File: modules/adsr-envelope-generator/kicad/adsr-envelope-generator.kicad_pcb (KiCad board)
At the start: 2 copper layers, 78 parts, among them P1 CONN_01X03, P2 CONN_01X02, P3 CONN_01X02, P4 CONN_01X03, Q1 Q_NPN_EBC, Q2 Q_NPN_EBC, Q3 Q_NPN_EBC, U1 TL074, U2 4066, U3 40106, U4 TL074, U5 4001

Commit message: ADSR PCB by freerouter
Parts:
- C1, C10, C11, C12, C13, C14, C15, C16, C17, C18, C19, C2, C20, C3, C4, C5, C6, C7, C8, C9, D1, D2, D3, D4, D5, D6, D7, D8, D9, P1, P2, P3, P4, Q1, Q2, Q3, R1, R10, R11, R12, R13, R14, R15, R16, R17, R18, R19, R2, R20, R21, R22, R23, R24, R25, R26, R27, R28, R29, R3, R30, R31, R32, R33, R4, R5, R6, R7, R8, R9, U1, U2, U3, U4, U5: moved to B.Cu
- moved R1 105.6 mm to (80.5, 98.8), turned to 270 degrees
- moved R2 99.5 mm to (82.5, 84.3), turned to 180 degrees
- moved R3 90.4 mm to (80.5, 90.4), turned to 270 degrees
- moved C15 88.3 mm to (83.3, 80.5)
- moved R4 84.2 mm to (80.5, 114.6), turned to 270 degrees
- moved R11 79.0 mm to (84.6, 90.7), turned to 270 degrees
- moved Q2 76.0 mm to (110.7, 84.3)
- moved U1 73.5 mm to (117.3, 100.1), turned to 270 degrees
- moved R12 72.8 mm to (84.6, 98.8), turned to 270 degrees
- moved R13 72.0 mm to (80.5, 106.7), turned to 270 degrees
- moved R8 71.2 mm to (84.3, 106.9), turned to 270 degrees
- moved R5 70.7 mm to (84.6, 114.6), turned to 270 degrees
- moved R28 64.7 mm to (115.6, 90.4), turned to 270 degrees
- moved R29 64.6 mm to (111.0, 100.1), turned to 270 degrees
- moved C13 64.5 mm to (127.3, 103.9)
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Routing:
- net GND: track 0.00 -> 328.3 mm, vias 0 -> 2
- net VCC: track 0.00 -> 225.0 mm, vias 0 -> 5
- net Net-(C3-Pad1): track 0.00 -> 139.8 mm, vias 0 -> 3
- net VEE: track 0.00 -> 133.0 mm, vias 0 -> 4
- net Net-(C5-Pad1): track 0.00 -> 132.2 mm, vias 0 -> 3
- net Net-(C4-Pad1): track 0.00 -> 120.9 mm, vias 0 -> 4
- net GateInput: track 0.00 -> 116.6 mm, vias 0 -> 2
- net OutputLevel: track 0.00 -> 114.3 mm, vias 0 -> 2
- net Net-(C5-Pad2): track 0.00 -> 105.8 mm, vias 0 -> 3
- net Net-(C9-Pad1): track 0.00 -> 103.1 mm, vias 0 -> 4
- net TriggerInput: track 0.00 -> 99.1 mm, vias 0 -> 1
- net ManTriggerBTN: track 0.00 -> 94.3 mm
- net Net-(Q1-Pad2): track 0.00 -> 90.8 mm, vias 0 -> 2
- net Net-(C2-Pad2): track 0.00 -> 86.4 mm, vias 0 -> 3
- net Net-(D3-Pad2): track 0.00 -> 84.4 mm, vias 0 -> 2
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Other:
- board outline added: 73.2 x 49.8 mm

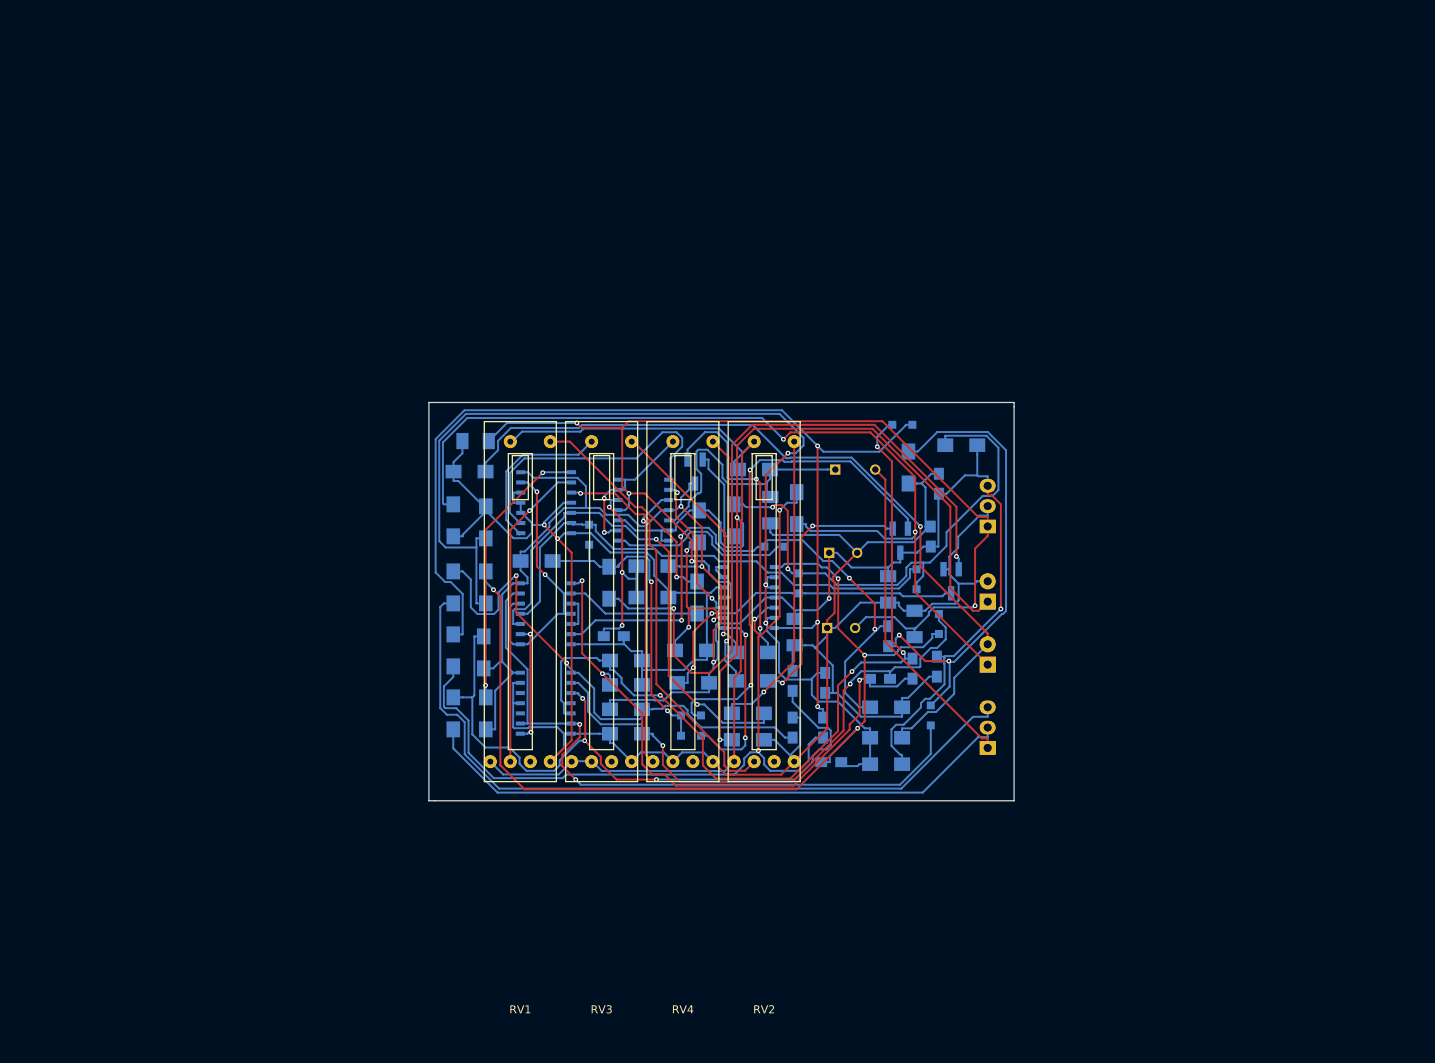
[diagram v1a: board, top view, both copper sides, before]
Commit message: Redo ADSR generator PCB layout
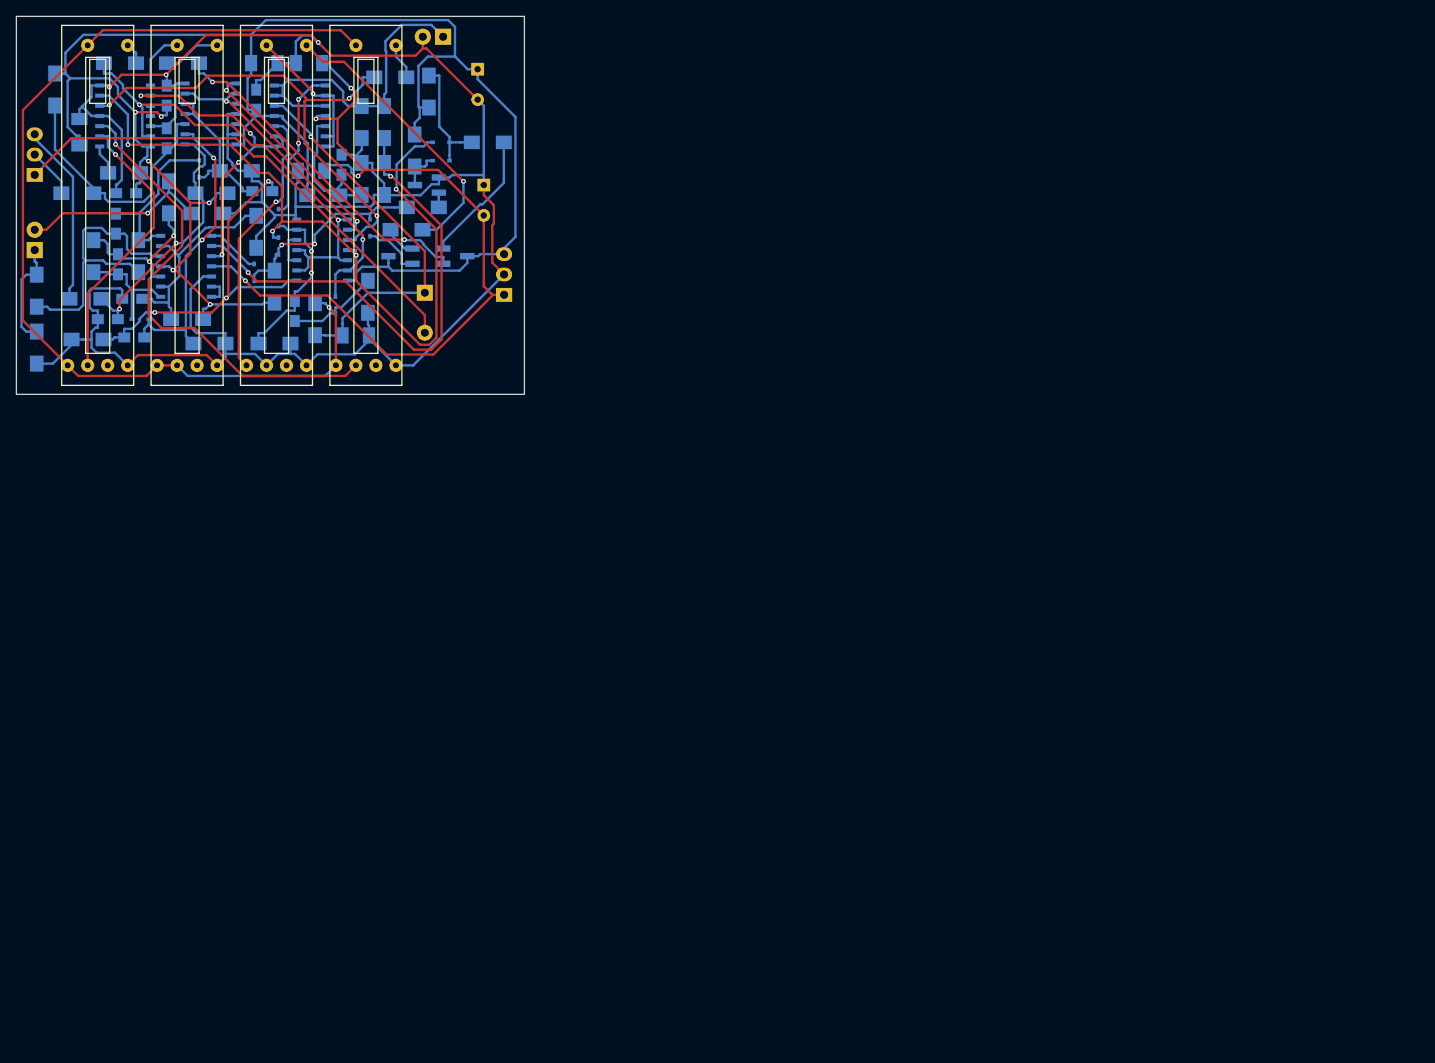
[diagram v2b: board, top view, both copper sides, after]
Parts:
- C12, C13: footprint Capacitors_ThroughHole:C_Radial_D8_L11.5_P3.5 -> Capacitors_ThroughHole:CP_Radial_D8.0mm_P3.80mm
- C8: footprint Capacitors_ThroughHole:C_Radial_D10_L13_P5 -> Capacitors_ThroughHole:CP_Radial_D10.0mm_P5.00mm
- D1, D2, D3, D4, D5, D6, D7, D8, D9: footprint Diodes_SMD:SOD-323_HandSoldering -> Diodes_SMD:SOD-323
- moved P1 139.0 mm to (28.2, 47.2)
- moved P2 129.9 mm to (28.2, 56.6)
- moved C18 119.8 mm to (44.7, 37.3), turned to 270 degrees
- moved C16 116.1 mm to (33.8, 41.9), turned to 90 degrees
- moved R9 112.3 mm to (45.0, 50.0), turned to 90 degrees
- moved C19 109.4 mm to (39.6, 49.5), turned to 0 degrees
- moved C4 108.7 mm to (38.6, 58.4), turned to 90 degrees
- moved C5 108.5 mm to (38.4, 53.3)
- moved D1 106.8 mm to (41.4, 65.3), turned to 180 degrees
- moved R6 103.6 mm to (47.2, 65.3)
- moved C2 103.5 mm to (44.7, 42.7)
- moved C7 102.5 mm to (40.6, 67.6)
- moved R30 102.4 mm to (46.7, 33.3)
- moved C9 100.8 mm to (56.6, 49.3), turned to 0 degrees
- moved C1 99.7 mm to (37.3, 65.3), turned to 0 degrees
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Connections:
- C4 pad 2: Net-(C3-Pad1) -> Net-(C4-Pad2)
- R12 pad 2: Net-(C3-Pad1) -> Net-(C4-Pad2)
- R9 pad 1: Net-(C3-Pad1) -> Net-(C4-Pad2)
- U1 pad 3: Net-(C3-Pad1) -> Net-(C4-Pad2)
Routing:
- net Net-(C3-Pad1): track 139.8 -> 27.8 mm, vias 3 -> 0
- net Net-(C5-Pad1): track 132.2 -> 21.2 mm, vias 3 -> 0
- net Net-(C4-Pad1): track 120.9 -> 14.1 mm, vias 4 -> 0
- net GateInput: track 116.6 -> 13.4 mm, vias 2 -> 0
- net Net-(Q1-Pad2): track 90.8 -> 1.85 mm, vias 2 -> 0
- net Net-(C9-Pad1): track 103.1 -> 20.2 mm, vias 4 -> 0
- net TriggerInput: track 99.1 -> 24.1 mm
- net OutputLevel: track 114.3 -> 41.1 mm, vias 2 -> 0
- net ManTriggerBTN: track 94.3 -> 22.7 mm
- net Net-(C5-Pad2): track 105.8 -> 35.2 mm, vias 3 -> 0
- net ManGateBTN: track 75.5 -> 6.21 mm
- net Net-(D9-Pad1): track 62.4 -> 7.47 mm, vias 2 -> 0
- net Net-(C2-Pad2): track 86.4 -> 33.0 mm, vias 3 -> 0
- net Net-(C10-Pad1): track 74.2 -> 22.0 mm, vias 4 -> 2
- net Net-(D5-Pad2): track 65.7 -> 15.3 mm, vias 2 -> 0
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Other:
- board size 73.2 x 49.8 mm -> 63.5 x 47.2 mm
- net class Default: clearance 0.2 -> 0.3; trace_width 0.25 -> 0.3
- rule pad_to_mask_clearance: 0.2 -> 0
- rule trace_clearance: 0.2 -> 0.3
- board text added: "+"
- board text added: "-"
- board text added: "0"
- board text added: "ADSR EG MICHD, JAN 2017"
- board text added: "ADSR OUT"
- board text added: "BASED ON RAY WILSON'S CIRCUIT DESIGN"
- board text added: "GateIn"
- board text added: "Lsw"
- board text added: "TrigIn"
- board text added: "mG"
- board text added: "mT"

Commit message: Finish up ADSR generator schematic, PCB, replace broken one
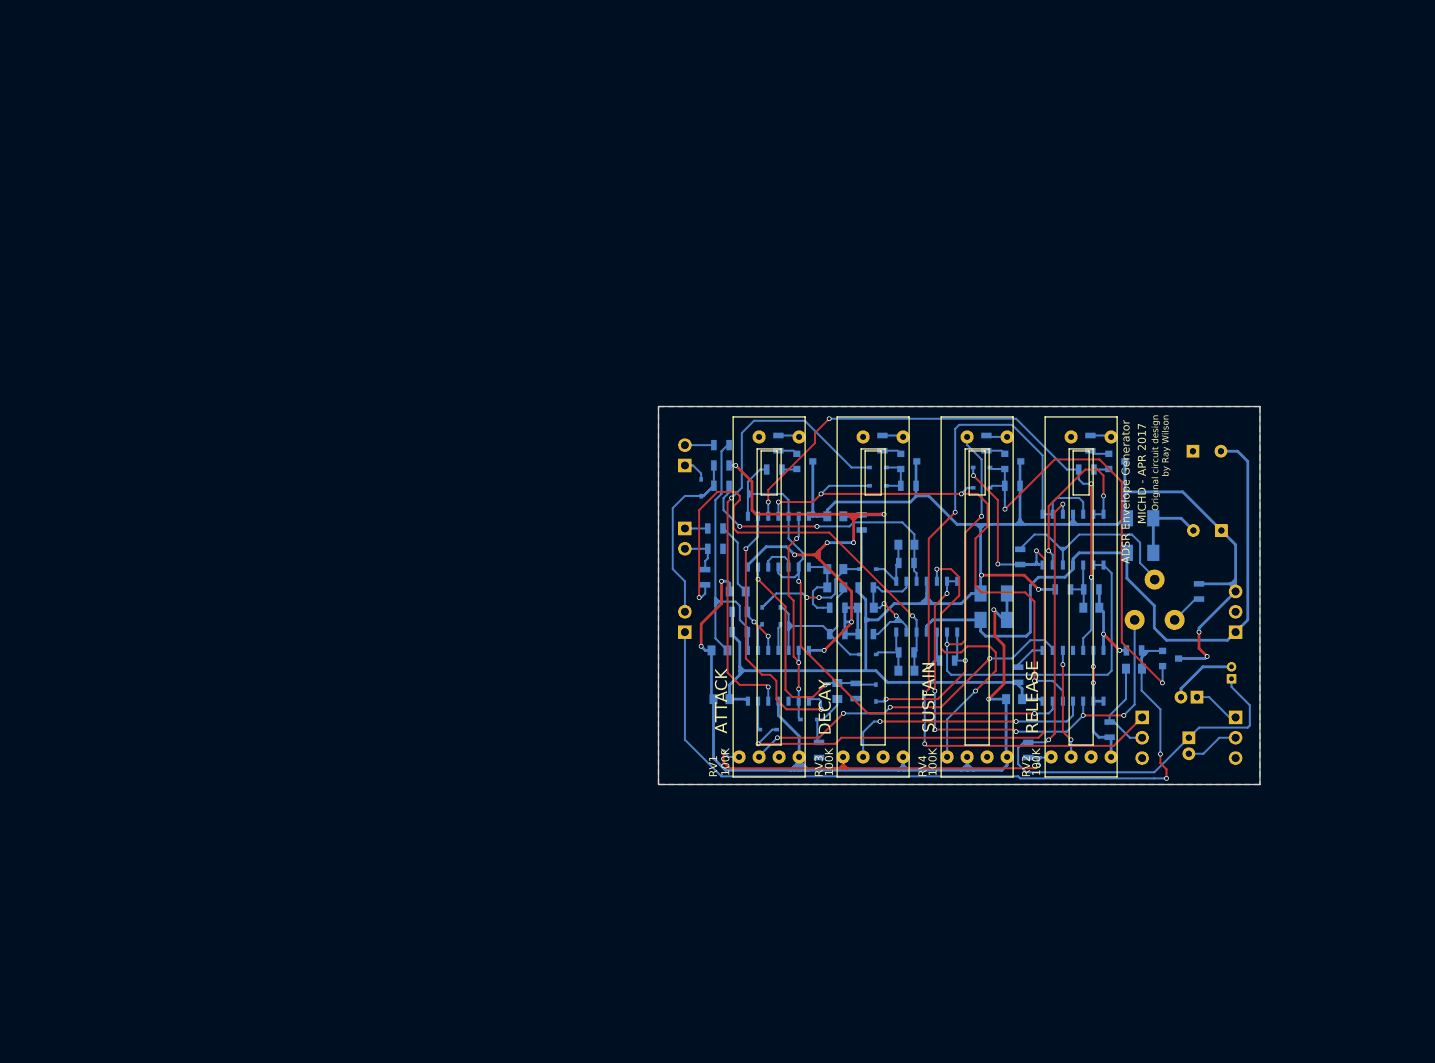
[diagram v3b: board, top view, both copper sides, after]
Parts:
- added C21: 10n, Capacitors_SMD:C_0805, B.Cu at (165.6, 109.0)
- added C22: 100n, Capacitors_SMD:C_0805, B.Cu at (114.0, 112.8)
- added D10: 1N4148, Diodes_SMD:SOD-323, B.Cu at (146.6, 83.8)
- added D11: 1N4148, Diodes_SMD:SOD-323, B.Cu at (146.6, 86.4)
- added D12: 1N4148, Diodes_SMD:SOD-323, B.Cu at (111.5, 86.4)
- added P5: CONN_01X03, Pin_Headers:Pin_Header_Straight_1x03_Pitch2.54mm, B.Cu at (166.6, 115.1)
- added P6: CONN_01X02, Pin_Headers:Pin_Header_Straight_1x02_Pitch2.54mm, B.Cu at (109.5, 104.4)
- added Q4: MMBT3904, TO_SOT_Packages_SMD:SOT-23, B.Cu at (150.5, 83.1)
- added Q5: MMBT3904, TO_SOT_Packages_SMD:SOT-23, B.Cu at (163.5, 83.1)
- added R34: 220R, Resistors_SMD:R_0805, B.Cu at (160.2, 80.8)
- added RV5: 10K, Potentiometers:Potentiometer_Triwood_RM-065, B.Cu at (170.7, 102.9)
- C1, C19, C2, C20, C3, C4, C5, C7: footprint Capacitors_SMD:C_0805_HandSoldering -> Capacitors_SMD:C_0805
- C10: value 1n -> 47u; footprint Capacitors_SMD:C_0805_HandSoldering -> Capacitors_ThroughHole:CP_Radial_D5.0mm_P2.00mm
- C11: value 100n -> 1n; footprint Capacitors_SMD:C_0805_HandSoldering -> Capacitors_SMD:C_0805
- C12, C13: footprint Capacitors_ThroughHole:CP_Radial_D8.0mm_P3.80mm -> Capacitors_ThroughHole:CP_Radial_D8.0mm_P3.50mm
- C14: value 10u -> 100n; footprint SMD_Packages:SMD-1206_Pol -> Capacitors_SMD:C_0805
- C18: value 100n -> 10u; footprint Capacitors_SMD:C_0805_HandSoldering -> SMD_Packages:SMD-1206_Pol
- C6: value 10u -> 3.3u; footprint SMD_Packages:SMD-1206_Pol -> Capacitors_ThroughHole:CP_Radial_D4.0mm_P1.50mm
- C8: value 220u -> 10n; footprint Capacitors_ThroughHole:CP_Radial_D10.0mm_P5.00mm -> Capacitors_SMD:C_0805
- C9: value 1n -> 100u; footprint Capacitors_SMD:C_0805_HandSoldering -> Capacitors_ThroughHole:CP_Radial_D5.0mm_P2.00mm
- P1: value CONN_01X03 -> CONN_01X02; footprint Pin_Headers:Pin_Header_Straight_1x03 -> Pin_Headers:Pin_Header_Straight_1x02_Pitch2.54mm
- P2: footprint Pin_Headers:Pin_Header_Straight_1x02 -> Pin_Headers:Pin_Header_Straight_1x02_Pitch2.54mm
- P3: value CONN_01X02 -> CONN_01X03; footprint Pin_Headers:Pin_Header_Straight_1x02 -> Pin_Headers:Pin_Header_Straight_1x03_Pitch2.54mm
- P4: footprint Pin_Headers:Pin_Header_Straight_1x03 -> Pin_Headers:Pin_Header_Straight_1x03_Pitch2.54mm
- Q1, Q2, Q3: value Q_NPN_EBC -> MMBT3904; footprint TO_SOT_Packages_SMD:SOT-23_Handsoldering -> TO_SOT_Packages_SMD:SOT-23
- R1: value 1K -> 100R; footprint Resistors_SMD:R_1206_HandSoldering -> Resistors_SMD:R_0805
- R10, R9: value 20K -> 10K; footprint Resistors_SMD:R_1206_HandSoldering -> Resistors_SMD:R_0805
- R11, R12, R13, R14, R15, R16, R17, R18, R19, R2, R25, R27, R28, R3, R31, R32, R8: footprint Resistors_SMD:R_1206_HandSoldering -> Resistors_SMD:R_0805
- R20: value 100K -> 1M; footprint Resistors_SMD:R_1206_HandSoldering -> Resistors_SMD:R_0805
- R21: value 100K -> 10K; footprint Resistors_SMD:R_1206_HandSoldering -> Resistors_SMD:R_0805
- R22: value 2K2 -> 33K; footprint Resistors_SMD:R_1206_HandSoldering -> Resistors_SMD:R_0805
- R23, R26: value 10K -> 100K; footprint Resistors_SMD:R_1206_HandSoldering -> Resistors_SMD:R_0805
- R24: value 82K -> 1M; footprint Resistors_SMD:R_1206_HandSoldering -> Resistors_SMD:R_0805
- R29, R30: value 220R -> 10K; footprint Resistors_SMD:R_1206_HandSoldering -> Resistors_SMD:R_0805
- R33: value 10K -> 220R; footprint Resistors_SMD:R_1206_HandSoldering -> Resistors_SMD:R_0805
- R4: value 1K -> 33K; footprint Resistors_SMD:R_1206_HandSoldering -> Resistors_SMD:R_0805
- R5: value 100R -> 1K; footprint Resistors_SMD:R_1206_HandSoldering -> Resistors_SMD:R_0805
- R6: value 33K -> 22K; footprint Resistors_SMD:R_1206_HandSoldering -> Resistors_SMD:R_0805
- R7: value 1K -> 22K; footprint Resistors_SMD:R_1206_HandSoldering -> Resistors_SMD:R_0805
- RV1, RV2, RV3, RV4: value LED-POT -> 100K; footprint Bourns PTL:Bourns PTL30-X -> Bourns PTL:Bourns-PTL30-X
- U1: value TL074 -> 4066
- U2: value 4066 -> TL974
- U4: value TL074 -> 4001
- U5: value 4001 -> TL974
- moved C9 134.5 mm to (172.5, 117.6), turned to 270 degrees
- moved C18 134.4 mm to (166.4, 94.5), turned to 180 degrees
- moved P3 130.6 mm to (178.3, 115.1), turned to 180 degrees
- moved C16 129.5 mm to (148.1, 102.9), turned to 180 degrees
- moved R1 125.7 mm to (151.1, 109.7), turned to 90 degrees
- moved C14 123.8 mm to (160.3, 101.3)
- moved C10 122.7 mm to (173.5, 112.5), turned to 180 degrees
- moved U1 122.1 mm to (158.0, 110.0), turned to 0 degrees
- moved C20 120.8 mm to (150.6, 112.8), turned to 180 degrees
- moved R26 118.2 mm to (162.6, 116.6), turned to 270 degrees
- moved C6 117.6 mm to (177.8, 110.2), turned to 90 degrees
- moved U2 117.4 mm to (139.7, 101.3), turned to 0 degrees
- moved R30 116.4 mm to (150.4, 86.1), turned to 180 degrees
- moved C5 113.5 mm to (137.2, 109.2), turned to 180 degrees
- moved C17 112.4 mm to (166.4, 90.2)
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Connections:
- C1 pad 1: GND -> Net-(C1-Pad1)
- C1 pad 2: Net-(C1-Pad2) -> GND
- C10 pad 2: Net-(C10-Pad2) -> GND
- C11 pad 1: GND -> Net-(C11-Pad1)
- C14 pad 1: VCC -> Net-(C14-Pad1)
- C15 pad 1: GND -> VCC
- C15 pad 2: VEE -> GND
- C16 pad 1: VCC -> GND
- C16 pad 2: GND -> VEE
- C17 pad 1: GND -> VCC
- C17 pad 2: VEE -> GND
- C18 pad 2: VCC -> VEE
- C19 pad 1: GND -> VCC
- C19 pad 2: VCC -> GND
- C2 pad 1: GND -> Net-(C2-Pad1)
- C2 pad 2: Net-(C2-Pad2) -> GND
- C20 pad 1: GND -> VCC
- C20 pad 2: VCC -> GND
- C8 pad 1: Net-(C6-Pad1) -> Net-(C8-Pad1)
- C8 pad 2: LongTimesSW -> Net-(C7-Pad2)
- C9 pad 1: Net-(C9-Pad1) -> Net-(C6-Pad1)
- C9 pad 2: Net-(C7-Pad1) -> Net-(C9-Pad2)
- D1 pad 1: Net-(C7-Pad2) -> Net-(C7-Pad1)
- D1 pad 2: Net-(C4-Pad1) -> Net-(C4-Pad2)
- D2 pad 1: Net-(C9-Pad1) -> Net-(C8-Pad1)
- D2 pad 2: Net-(C5-Pad1) -> Net-(C5-Pad2)
- D3 pad 1: Net-(C10-Pad2) -> Net-(C7-Pad1)
- D4 pad 1: Net-(C10-Pad1) -> Net-(C8-Pad1)
- D5 pad 1: Net-(D5-Pad1) -> Net-(C11-Pad1)
- D6 pad 1: Net-(D6-Pad1) -> Net-(C11-Pad2)
- D6 pad 2: SustainState -> Net-(D6-Pad2)
- D7 pad 1: SustainState -> Net-(D7-Pad1)
- D7 pad 2: DecayState -> Net-(D10-Pad1)
- D8 pad 1: DecayState -> Net-(D8-Pad1)
- D8 pad 2: Net-(D5-Pad2) -> Net-(D8-Pad2)
- D9 pad 1: Net-(D9-Pad1) -> DecayState
- D9 pad 2: SustainState -> Net-(D8-Pad2)
- P1 pad 1: LongTimesSW -> Net-(P1-Pad1)
- P1 pad 2: ManGateBTN -> Net-(P1-Pad2)
- P2 pad 1: GateInput -> Net-(D12-Pad2)
- P2 pad 2: TriggerInput -> Net-(P2-Pad2)
- P3 pad 1: OutputLevel -> Net-(C10-Pad1)
- P3 pad 2: GND -> Net-(C9-Pad2)
- Q1 pad 1: GND -> Net-(D10-Pad2)
- Q1 pad 2: Net-(Q1-Pad2) -> RetrigSW
- Q1 pad 3: Net-(D5-Pad1) -> VCC
- Q3 pad 1: Net-(Q3-Pad1) -> Net-(D8-Pad2)
- Q3 pad 2: Net-(D9-Pad1) -> Net-(Q3-Pad2)
- R1 pad 1: Net-(C1-Pad2) -> VCC
- R1 pad 2: ManTriggerBTN -> Net-(R1-Pad2)
- R10 pad 1: Net-(C5-Pad2) -> Net-(C3-Pad1)
- R10 pad 2: GateInput -> VCC
- R11 pad 1: GND -> Net-(C1-Pad1)
- R11 pad 2: Net-(C3-Pad1) -> GND
- R14 pad 1: Net-(C6-Pad1) -> Net-(R14-Pad1)
- R14 pad 2: Net-(R14-Pad2) -> Net-(C6-Pad1)
- R15 pad 1: Net-(C7-Pad2) -> Net-(C7-Pad1)
- R16 pad 1: Net-(C9-Pad1) -> GND
- R16 pad 2: GND -> Net-(C8-Pad1)
- R17 pad 1: Net-(C7-Pad1) -> Net-(C7-Pad2)
- R18 pad 1: Net-(C10-Pad2) -> Net-(C11-Pad1)
- R19 pad 1: Net-(C10-Pad1) -> Net-(C11-Pad2)
- R2 pad 1: TriggerInput -> GND
- R2 pad 2: GND -> TriggerInput
- R20 pad 1: VCC -> AdsrLevel
- R20 pad 2: Net-(C11-Pad2) -> Net-(D6-Pad2)
- R21 pad 1: Net-(C11-Pad2) -> VCC
- R21 pad 2: GND -> Net-(C14-Pad1)
- R22 pad 1: OutputLevel -> Net-(C14-Pad1)
- R22 pad 2: Net-(R22-Pad2) -> GND
- R23 pad 1: Net-(Q1-Pad2) -> VCC
- R23 pad 2: SustainState -> Net-(R23-Pad2)
- R24 pad 1: Net-(R22-Pad2) -> Net-(D10-Pad1)
- R24 pad 2: GND -> Net-(R24-Pad2)
- R25 pad 1: Net-(D5-Pad1) -> RetrigSW
- R25 pad 2: VCC -> GND
- R26 pad 1: VCC -> TrigOut
- R26 pad 2: SustainState -> GND
- R27 pad 1: Net-(D5-Pad2) -> AttackState
- R27 pad 2: VCC -> Net-(Q2-Pad1)
- R28 pad 1: Net-(D5-Pad2) -> ReleaseState
- R28 pad 2: Net-(Q2-Pad2) -> Net-(Q5-Pad1)
- R29 pad 1: A-LED -> VCC
- R29 pad 2: AttackState -> Net-(D8-Pad2)
- R3 pad 1: GateInput -> GND
- R3 pad 2: GND -> Net-(P1-Pad2)
- R30 pad 1: D-LED -> VCC
- R30 pad 2: Net-(Q2-Pad1) -> Net-(D10-Pad2)
- R31 pad 1: S-LED -> A-LED
- R31 pad 2: Net-(Q3-Pad1) -> Net-(Q2-Pad2)
- R32 pad 1: R-LED -> D-LED
- R32 pad 2: ReleaseState -> Net-(Q3-Pad2)
- R33 pad 1: OutputLevel -> S-LED
- R33 pad 2: GND -> Net-(Q4-Pad2)
- R4 pad 1: Net-(C2-Pad2) -> VCC
- R4 pad 2: ManGateBTN -> Net-(C1-Pad1)
- R5 pad 1: Net-(R5-Pad1) -> Net-(C2-Pad1)
- R5 pad 2: VCC -> Net-(P2-Pad2)
- R6 pad 1: Net-(C3-Pad1) -> TriggerInput
- R6 pad 2: VCC -> Net-(C4-Pad1)
- R7 pad 1: Net-(C1-Pad2) -> Net-(P1-Pad2)
- R7 pad 2: VCC -> Net-(C5-Pad1)
- R8 pad 1: Net-(C2-Pad2) -> Net-(C3-Pad1)
- R8 pad 2: VCC -> Net-(P1-Pad1)
- R9 pad 1: Net-(C4-Pad2) -> Net-(C2-Pad1)
- R9 pad 2: TriggerInput -> VCC
- RV1 pad 2: Net-(R14-Pad2) -> Net-(R14-Pad1)
- RV1 pad 3: Net-(R14-Pad2) -> Net-(RV1-Pad3)
- RV2 pad 2: Net-(R14-Pad2) -> Net-(R14-Pad1)
- RV2 pad 3: Net-(R14-Pad2) -> Net-(RV2-Pad3)
- RV3 pad 1: Net-(R14-Pad2) -> Net-(RV3-Pad1)
- RV3 pad 2: Net-(R14-Pad2) -> Net-(R14-Pad1)
- U1 pad 1: Net-(C4-Pad1) -> Net-(R1-Pad2)
- U1 pad 11: VEE -> Net-(RV3-Pad1)
- U1 pad 12: GND -> DecayState
- U1 pad 13: Net-(U1-Pad13) -> AttackState
- U1 pad 14: Net-(U1-Pad13) -> VCC
- U1 pad 2: Net-(C3-Pad1) -> Net-(RV1-Pad1)
- U1 pad 3: Net-(C4-Pad2) -> Net-(RV2-Pad1)
- U1 pad 4: VCC -> GND
- U1 pad 5: Net-(C5-Pad2) -> ReleaseState
- U1 pad 6: Net-(C3-Pad1) -> GND
- U1 pad 7: Net-(C5-Pad1) -> GND
- U1 pad 8: Net-(D6-Pad1) -> GND
- U1 pad 9: Net-(R22-Pad2) -> GND
- U2 pad 1: Net-(R5-Pad1) -> Net-(C4-Pad2)
- U2 pad 10: GND -> AdsrLevel
- U2 pad 11: GND -> VEE
- U2 pad 12: GND -> Net-(C5-Pad1)
- U2 pad 13: AttackState -> Net-(C1-Pad1)
- U2 pad 14: VCC -> Net-(C5-Pad2)
- U2 pad 2: Net-(RV1-Pad1) -> Net-(C1-Pad1)
- U2 pad 3: Net-(RV2-Pad1) -> Net-(C4-Pad1)
- U2 pad 4: GND -> VCC
- U2 pad 5: ReleaseState -> Net-(RV4-Pad2)
- U2 pad 6: DecayState -> SustainLevel
- U2 pad 7: GND -> SustainLevel
- U2 pad 8: Net-(RV3-Pad3) -> Net-(D6-Pad2)
- U2 pad 9: SustainLevel -> Net-(RV4-Pad3)
- U3 pad 1: Net-(C1-Pad2) -> Net-(C2-Pad1)
- U3 pad 12: Net-(U3-Pad12) -> Net-(D8-Pad1)
- U3 pad 13: GND -> Net-(D7-Pad1)
- U3 pad 2: Net-(C7-Pad2) -> Net-(D3-Pad2)
- U3 pad 3: Net-(C2-Pad2) -> Net-(C3-Pad1)
- U3 pad 4: Net-(C9-Pad1) -> Net-(D4-Pad2)
- U3 pad 5: Net-(C9-Pad1) -> Net-(C8-Pad1)
- U3 pad 6: Net-(D3-Pad2) -> Net-(D5-Pad2)
- U3 pad 9: Net-(D3-Pad2) -> Net-(D5-Pad2)
- U4 pad 1: SustainLevel -> Net-(C7-Pad2)
- U4 pad 10: OutputLevel -> ReleaseState
- U4 pad 11: VEE -> DecayState
- U4 pad 12: Net-(C11-Pad2) -> AttackState
- U4 pad 13: Net-(RV4-Pad3) -> Net-(D5-Pad2)
- U4 pad 14: Net-(RV4-Pad3) -> VCC
- U4 pad 2: SustainLevel -> AttackState
- U4 pad 3: Net-(RV4-Pad2) -> Net-(U4-Pad3)
- U4 pad 4: VCC -> AttackState
- U4 pad 5: Net-(C6-Pad1) -> Net-(U4-Pad3)
- U4 pad 6: OutputLevel -> Net-(C11-Pad2)
- U4 pad 7: OutputLevel -> GND
- U4 pad 8: Net-(D4-Pad2) -> AttackState
- U4 pad 9: Net-(RV4-Pad3) -> Net-(U3-Pad8)
- U5 pad 1: Net-(C7-Pad1) -> AdsrLevel
- U5 pad 10: ReleaseState -> Net-(C14-Pad1)
- U5 pad 11: DecayState -> VEE
- U5 pad 12: AttackState -> Net-(R24-Pad2)
- U5 pad 13: Net-(D3-Pad2) -> Net-(U5-Pad13)
- U5 pad 14: VCC -> Net-(D10-Pad1)
- U5 pad 2: AttackState -> AdsrLevel
- U5 pad 3: Net-(U5-Pad3) -> Net-(C6-Pad1)
- U5 pad 4: AttackState -> VCC
- U5 pad 5: Net-(U5-Pad3) -> AdsrLevel
- U5 pad 6: Net-(C10-Pad1) -> Net-(U5-Pad13)
- U5 pad 7: GND -> Net-(U5-Pad13)
- U5 pad 8: AttackState -> Net-(RV4-Pad3)
- U5 pad 9: Net-(U3-Pad8) -> Net-(RV4-Pad3)
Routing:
- net Net-(R14-Pad2): track 126.1 -> 0.00 mm, vias 1 -> 0
- net AdsrLevel: track 0.00 -> 103.7 mm, vias 0 -> 4
- net RetrigSW: track 0.00 -> 100.6 mm, vias 0 -> 2
- net Net-(D10-Pad1): track 0.00 -> 86.4 mm, vias 0 -> 4
- net Net-(R22-Pad2): track 63.3 -> 0.00 mm, vias 2 -> 0
- net LongTimesSW: track 62.0 -> 0.00 mm
- net Net-(D8-Pad1): track 0.00 -> 57.3 mm, vias 0 -> 2
- net Net-(D10-Pad2): track 0.00 -> 56.6 mm, vias 0 -> 2
- net Net-(R14-Pad1): track 0.00 -> 56.3 mm, vias 0 -> 2
- net GND: track 308.9 -> 256.5 mm, vias 3 -> 15
- net Net-(RV4-Pad3): track 19.5 -> 70.2 mm, vias 1 -> 2
- net Net-(RV2-Pad1): track 59.8 -> 13.7 mm, vias 1 -> 2
- net OutputLevel: track 41.1 -> 0.00 mm
- net Net-(Q2-Pad1): track 42.3 -> 1.89 mm, vias 2 -> 0
- net Net-(C2-Pad1): track 0.00 -> 38.6 mm
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- added copper zone on B.Cu, net GND
- added copper zone on F.Cu, net GND
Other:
- board size 63.5 x 47.2 mm -> 75.2 x 47.2 mm
- net class Default: clearance 0.3 -> 0.2; trace_width 0.3 -> 0.25
- net class Power added: clearance 0.25, trace_width 0.35, via_dia 0.6, via_drill 0.4
- rule pad_to_mask_clearance: 0 -> 0.2
- rule trace_clearance: 0.3 -> 0.2
- board text added: "+5V"
- board text added: "-5V"
- board text added: "ADSR Envelope Generator"
- board text added: "ADSR Out"
- board text added: "ATTACK"
- board text added: "DECAY"
- board text added: "Gate In"
- board text added: "MICHD - APR 2017"
- board text added: "Man Gate"
- board text added: "Man Trig"
- board text added: "Original circuit design by Ray Wilson"
- board text added: "RELEASE"
- board text added: "Retrig SW"
- board text added: "SUSTAIN"
- board text added: "TimeSel SW"
- board text added: "Trig In"
- board text added: "Trig Out"
- board text added: "^"
- board text removed: "+"
- board text removed: "-"
- board text removed: "0"
- board text removed: "ADSR EG MICHD, JAN 2017"
- board text removed: "ADSR OUT"
- board text removed: "BASED ON RAY WILSON'S CIRCUIT DESIGN"
- board text removed: "GateIn"
- board text removed: "Lsw"
- board text removed: "TrigIn"
- board text removed: "mG"
- board text removed: "mT"
